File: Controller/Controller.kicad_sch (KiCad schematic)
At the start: 13 parts, among them J1 12Vin, J2 12V_underside, J3 Sensor_VCC_GND, J4 Sensor_1_2, J5 Sensor_3_4, J6 Relayboard, J7 RTC, J8 Buttons, U1 DOIT-ESP32-DEVKIT-V1

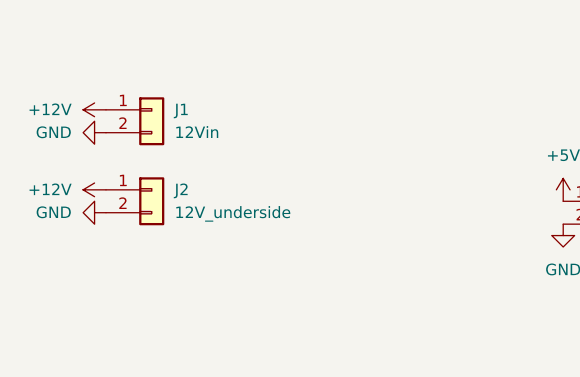
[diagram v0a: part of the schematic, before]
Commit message: switched 12V input pins for better routing
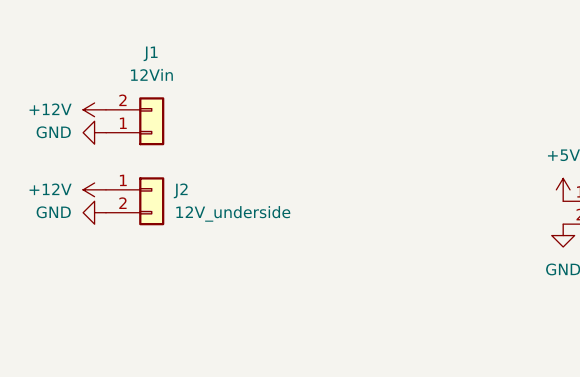
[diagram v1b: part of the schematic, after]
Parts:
- H1, H2, H3, H4: footprint MountingHole:MountingHole_3.2mm_M3 -> (none)
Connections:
- net +12V: now also J1.2 (Pin_2); no longer J1.1 (Pin_1)
- net GND: now also J1.1 (Pin_1); no longer J1.2 (Pin_2)
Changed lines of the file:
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@@
       (effects (font (size 1.27 1.27)) (justify left))
     )
-    (property "Footprint" "MountingHole:MountingHole_3.2mm_M3" (id 2) (at 273.228 39.4813 0)
+    (property "Footprint" "" (id 2) (at 273.228 39.4813 0)
       (effects (font (size 1.27 1.27)) hide)
     )
@@
     (pin "1")
   )
-  (symbol (lib_id "Connector_Generic:Conn_01x02") (at 34.29 33.02 0) (unit 1)
-    (in_bom yes) (on_board yes) (fields_autoplaced)
-    (property "Reference" "J1" (id 0) (at 36.83 33.0199 0)
-      (effects (font (size 1.27 1.27)) (justify left))
-    )
-    (property "Value" "12Vin" (id 1) (at 36.83 35.5599 0)
-      (effects (font (size 1.27 1.27)) (justify left))
-    )
-    (property "Footprint" "TerminalBlock:TerminalBlock_Altech_AK300-2_P5.00mm" (id 2) (at 34.29 33.02 0)
-      (effects (font (size 1.27 1.27)) hide)
-    )
-    (property "Datasheet" "~" (id 3) (at 34.29 33.02 0)
+  (symbol (lib_id "Connector_Generic:Conn_01x02") (at 34.29 35.56 0) (mirror x) (unit 1)
+    (in_bom yes) (on_board yes) (fields_autoplaced)
+    (property "Reference" "J1" (id 0) (at 34.29 26.67 0))
+    (property "Value" "12Vin" (id 1) (at 34.29 29.21 0))
+    (property "Footprint" "TerminalBlock:TerminalBlock_Altech_AK300-2_P5.00mm" (id 2) (at 34.29 35.56 0)
+      (effects (font (size 1.27 1.27)) hide)
+    )
+    (property "Datasheet" "~" (id 3) (at 34.29 35.56 0)
       (effects (font (size 1.27 1.27)) hide)
     )
@@
       (effects (font (size 1.27 1.27)) (justify left))
     )
-    (property "Footprint" "MountingHole:MountingHole_3.2mm_M3" (id 2) (at 273.05 66.04 0)
+    (property "Footprint" "" (id 2) (at 273.05 66.04 0)
       (effects (font (size 1.27 1.27)) hide)
     )
@@
       (effects (font (size 1.27 1.27)) (justify left))
     )
-    (property "Footprint" "MountingHole:MountingHole_3.2mm_M3" (id 2) (at 273.05 50.8 0)
+    (property "Footprint" "" (id 2) (at 273.05 50.8 0)
       (effects (font (size 1.27 1.27)) hide)
     )
@@
       (effects (font (size 1.27 1.27)) (justify left))
     )
-    (property "Footprint" "MountingHole:MountingHole_3.2mm_M3" (id 2) (at 273.05 25.4 0)
+    (property "Footprint" "" (id 2) (at 273.05 25.4 0)
       (effects (font (size 1.27 1.27)) hide)
     )
@@
     )
     (path "/e50812bf-0199-4ce8-96e2-2acd9a19f7c3"
-      (reference "H1") (unit 1) (value "MountingHole") (footprint "MountingHole:MountingHole_3.2mm_M3")
+      (reference "H1") (unit 1) (value "MountingHole") (footprint "MountingHole:MountingHole_3.2mm_M3_DIN965")
     )
     (path "/ccc300cc-1b9f-42a0-aa7a-badea07fb048"
-      (reference "H2") (unit 1) (value "MountingHole") (footprint "MountingHole:MountingHole_3.2mm_M3")
+      (reference "H2") (unit 1) (value "MountingHole") (footprint "MountingHole:MountingHole_3.2mm_M3_DIN965")
     )
     (path "/c783c1e1-2a32-4db3-8b0f-49522b837631"
-      (reference "H3") (unit 1) (value "MountingHole") (footprint "MountingHole:MountingHole_3.2mm_M3")
+      (reference "H3") (unit 1) (value "MountingHole") (footprint "MountingHole:MountingHole_3.2mm_M3_DIN965")
     )
     (path "/8e8e9b67-fbab-49f6-a241-642514fcb4ac"
-      (reference "H4") (unit 1) (value "MountingHole") (footprint "MountingHole:MountingHole_3.2mm_M3")
+      (reference "H4") (unit 1) (value "MountingHole") (footprint "MountingHole:MountingHole_3.2mm_M3_DIN965")
     )
     (path "/bff43975-a3f9-4dd6-bece-4a049028094c"

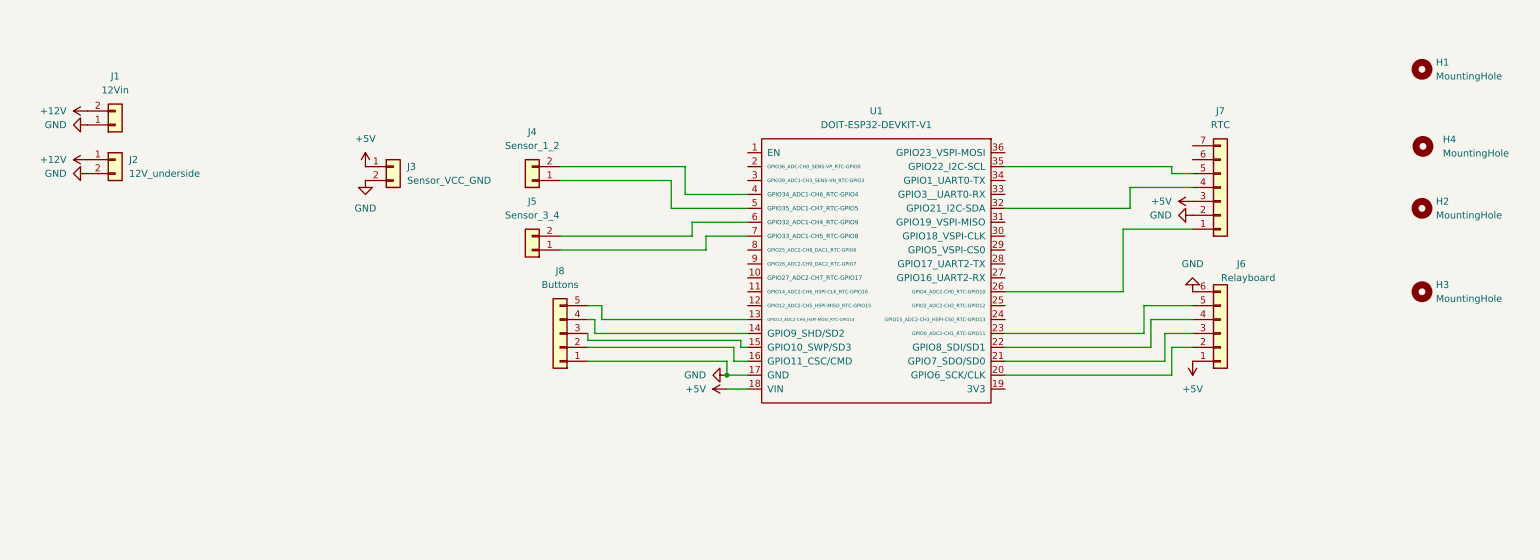
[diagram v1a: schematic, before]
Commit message: added Silkscreens, GND Polygons & more
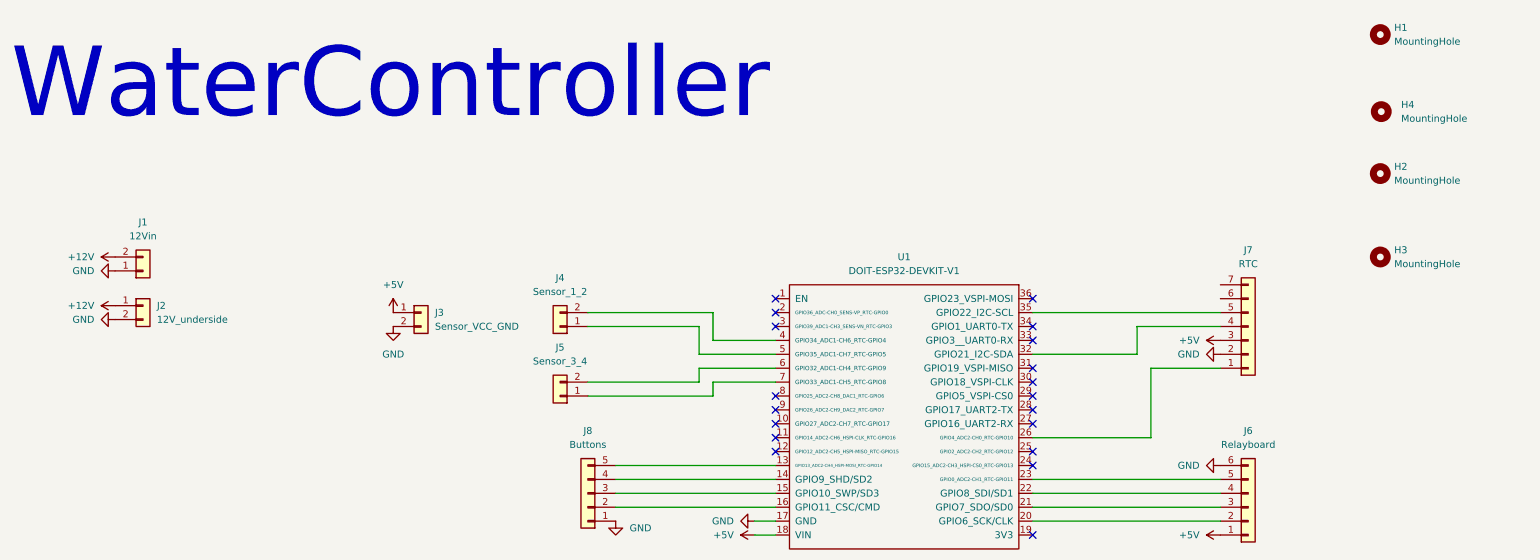
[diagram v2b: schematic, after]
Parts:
- H1, H2, H3, H4: footprint (none) -> MountingHole:MountingHole_3.2mm_M3_DIN965
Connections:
- no-connect marks 0 -> 19
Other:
- note added: "WaterController"
- company: (none) -> Exellent1988
- title: (none) -> WaterController
- moved on the sheet: H1, H2, H3, H4, J1, J2, J3, J4, J5, J6, J7, J8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
